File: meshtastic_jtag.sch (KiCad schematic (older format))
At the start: 19 parts, among them J2 JTAG, J4 usr_btn, J5 pcb antenna, U1 ESP32-DevKitC, U2 E22-900M22S, U3 OLED, U4 neo6m

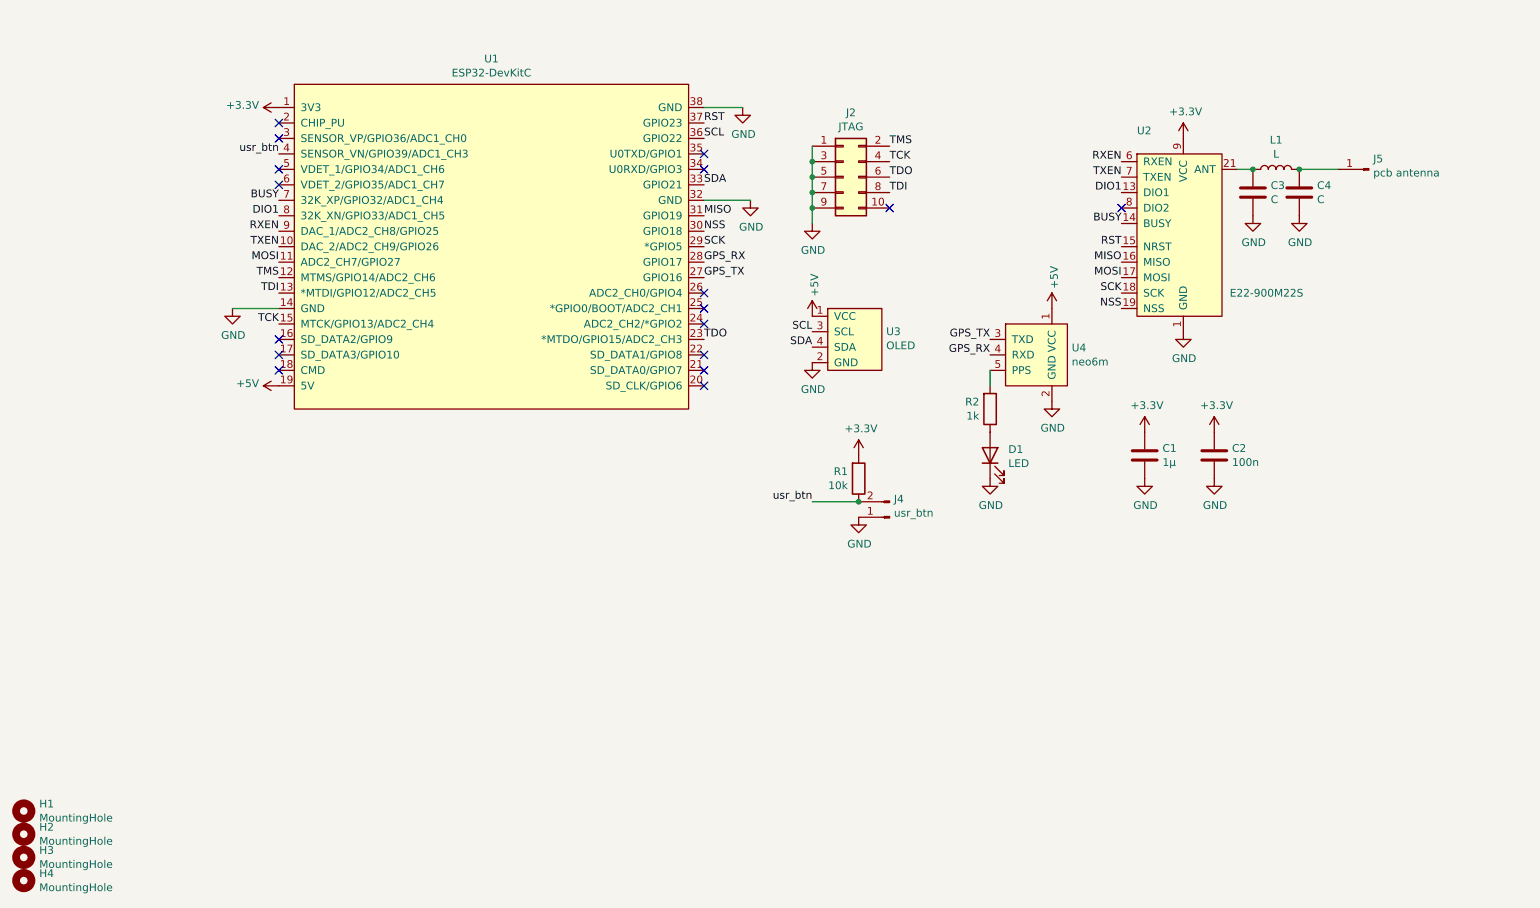
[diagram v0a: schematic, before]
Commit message: bump to V1.1, solder jumpers to swap OLED VCC/GND added
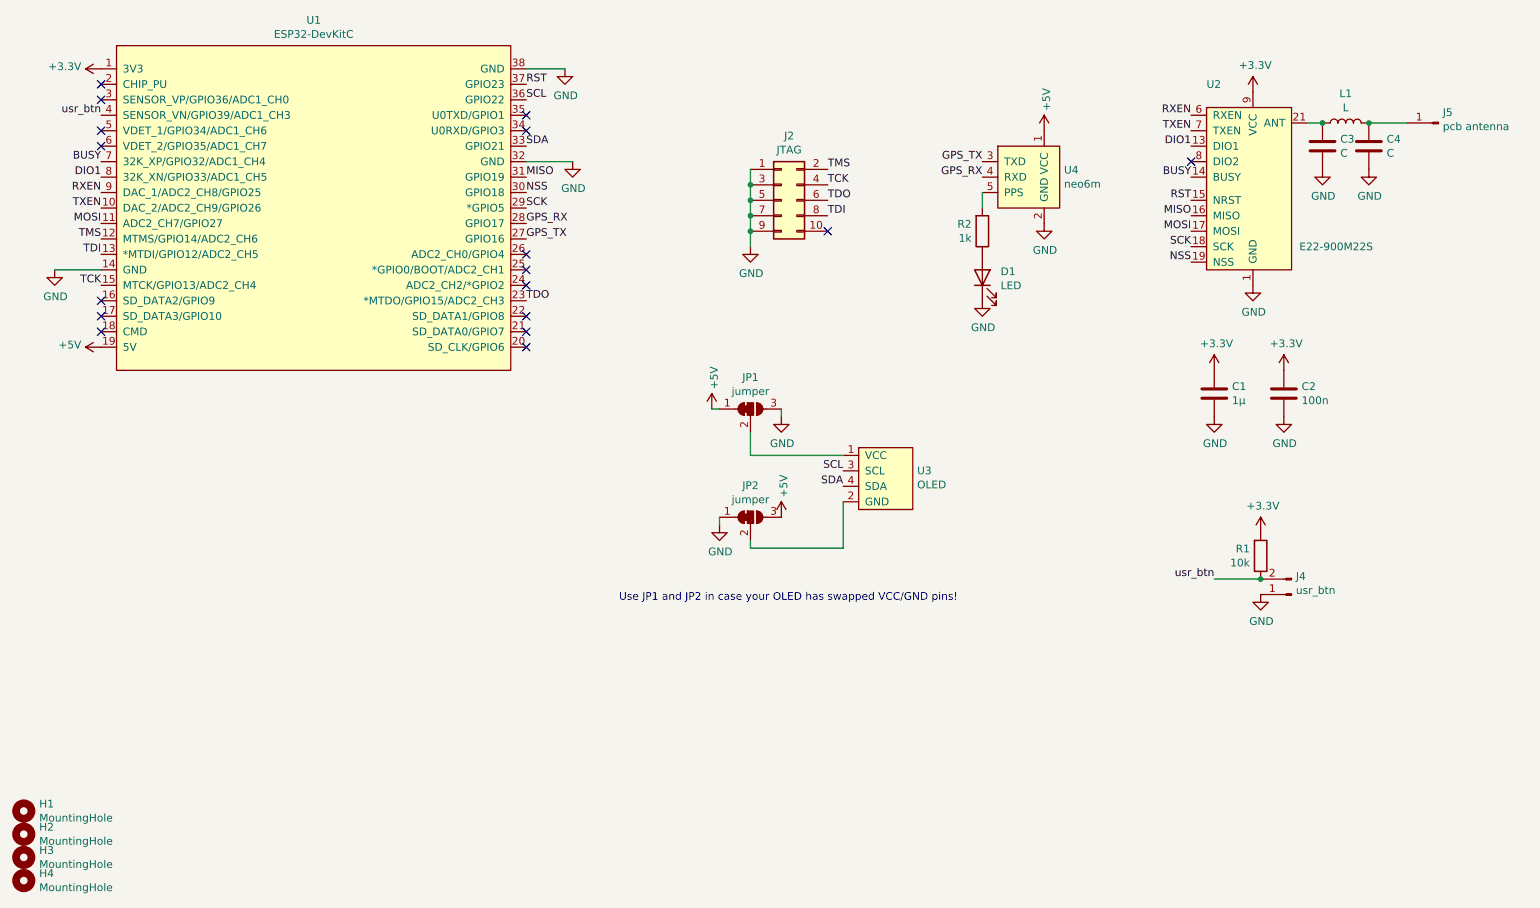
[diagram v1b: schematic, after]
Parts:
- added JP1, JP2: jumper, Jumper:SolderJumper-3_P1.3mm_Bridged12_Pad1.0x1.5mm_NumberLabels, symbol Jumper:SolderJumper_3_Bridged12
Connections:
- net +5V: now also JP1.1 (A), JP2.3 (B); no longer U3.1 (VCC)
- net GND: now also JP1.3 (B), JP2.1 (A); no longer U3.2 (GND)
- new net: JP1.2 (C), U3.1 (VCC)
- new net: JP2.2 (C), U3.2 (GND)
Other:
- note added: "Use JP1 and JP2 in case your OLED has swapped VCC/GND pins!"
- moved on the sheet: C1, C2, C3, C4, D1, J2, J4, J5, L1, R1, R2, U1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
